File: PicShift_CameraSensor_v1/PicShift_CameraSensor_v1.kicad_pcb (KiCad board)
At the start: 2 copper layers, 55.9 x 32 mm, 72 parts, among them J1 Conn_01x11, J2 Conn_01x11, U1 ADG732BSUZ, U2 ADG732BSUZ

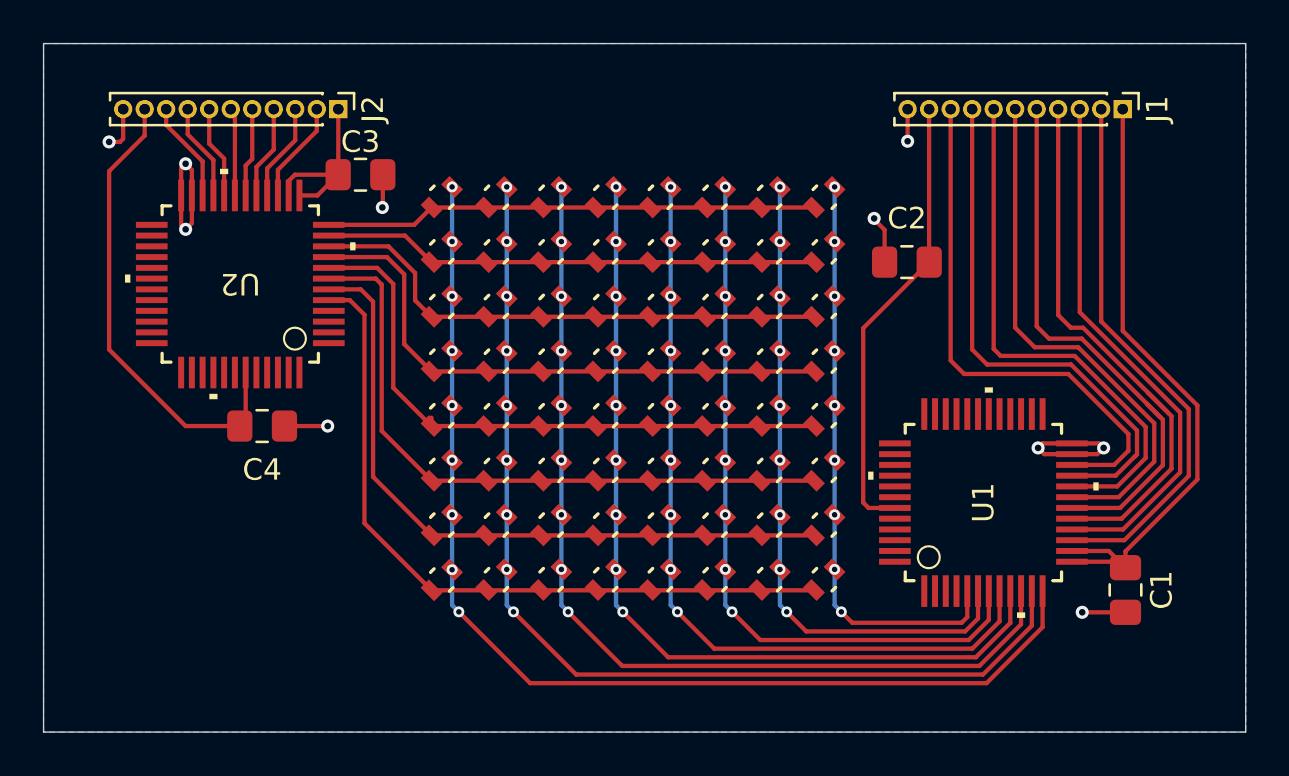
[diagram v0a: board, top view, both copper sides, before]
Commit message: updated shape of PCB
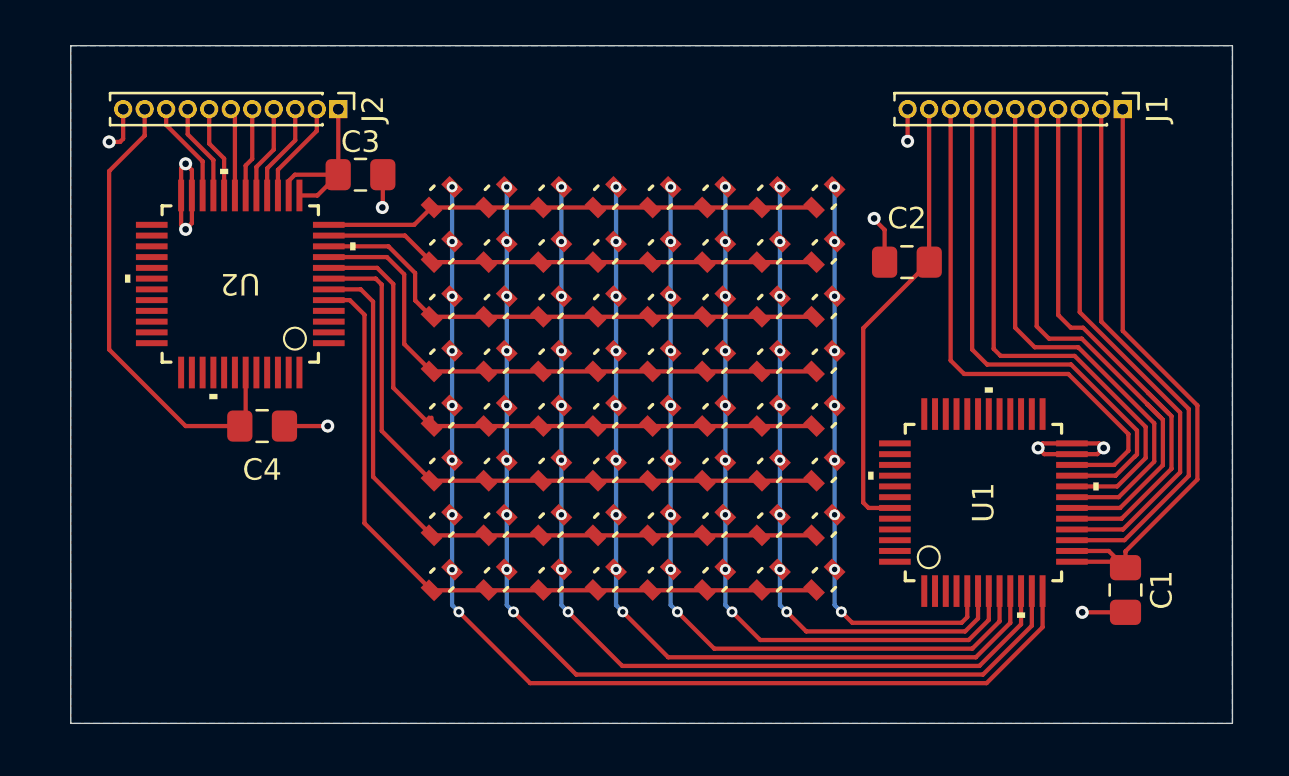
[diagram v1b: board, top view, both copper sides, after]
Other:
- board size 55.9 x 32 mm -> 54 x 31.5 mm
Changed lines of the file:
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@@
 		(layer "F.SilkS")
 	)
-	(gr_line
-		(start 46.736 57.404)
-		(end 46.736 25.4)
+	(gr_rect
+		(start 48 25.5)
+		(end 102 57)
 		(stroke
 			(width 0.05)
 			(type default)
 		)
-		(layer "Edge.Cuts")
-	)
-	(gr_line
-		(start 46.736 25.4)
-		(end 102.616 25.4)
-		(stroke
-			(width 0.05)
-			(type default)
-		)
-		(layer "Edge.Cuts")
-	)
-	(gr_line
-		(start 102.616 25.4)
-		(end 102.616 57.404)
-		(stroke
-			(width 0.05)
-			(type default)
-		)
-		(layer "Edge.Cuts")
-	)
-	(gr_line
-		(start 102.616 57.404)
-		(end 46.736 57.404)
-		(stroke
-			(width 0.05)
-			(type default)
-		)
+		(fill no)
 		(layer "Edge.Cuts")
 	)
@@
 		(polygon
 			(pts
-				(xy 46.736 25.4) (xy 102.616 25.4) (xy 102.616 57.404) (xy 46.736 57.404)
+				(xy 48 25.5) (xy 102 25.5) (xy 102 57) (xy 48 57)
 			)
 		)
